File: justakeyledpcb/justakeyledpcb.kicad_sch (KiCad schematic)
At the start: 14 parts, among them SW1 SW_Push, SW2 SW_Push, SW3 SW_Push, SW4 SW_Push, U1 XIAO-RP2040-DIP

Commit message: The Schematic is Finalised
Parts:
- added R5: R, Resistor_THT:R_Axial_DIN0207_L6.3mm_D2.5mm_P7.62mm_Horizontal, symbol Device:R
- BZ1: footprint (none) -> Buzzer_Beeper:Buzzer_12x9.5RM7.6
- D1, D2, D3, D4: footprint (none) -> footprints:LEDRD254W57D500H1070
- R1, R2, R3, R4: footprint (none) -> Resistor_THT:R_Axial_DIN0207_L6.3mm_D2.5mm_P7.62mm_Horizontal
- SW1, SW2, SW3, SW4: footprint (none) -> Button_Switch_Keyboard:SW_Cherry_MX_1.00u_PCB
- U1: footprint Module:MOUDLE14P-XIAO-DIP-SMD -> footprints:XIAO-RP2040-DIP
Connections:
- net Buzzer: now also R5.1; no longer BZ1.1 (+)
- new net: BZ1.1 (+), R5.2
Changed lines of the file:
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@@
 	(wire
 		(pts
-			(xy 162.56 72.39) (xy 167.64 72.39)
+			(xy 99.06 78.74) (xy 102.87 78.74)
 		)
 		(stroke
@@
 	(wire
 		(pts
-			(xy 99.06 78.74) (xy 102.87 78.74)
+			(xy 99.06 74.93) (xy 102.87 74.93)
 		)
 		(stroke
@@
 	(wire
 		(pts
-			(xy 99.06 74.93) (xy 102.87 74.93)
+			(xy 138.43 86.36) (xy 140.97 86.36)
 		)
 		(stroke
@@
 	(wire
 		(pts
-			(xy 138.43 86.36) (xy 140.97 86.36)
+			(xy 133.35 49.53) (xy 130.81 49.53)
 		)
 		(stroke
@@
 	(wire
 		(pts
-			(xy 133.35 49.53) (xy 130.81 49.53)
+			(xy 138.43 93.98) (xy 140.97 93.98)
 		)
 		(stroke
@@
 	(wire
 		(pts
-			(xy 138.43 93.98) (xy 140.97 93.98)
+			(xy 99.06 82.55) (xy 102.87 82.55)
 		)
 		(stroke
@@
 	(wire
 		(pts
-			(xy 99.06 82.55) (xy 102.87 82.55)
+			(xy 138.43 74.93) (xy 146.05 74.93)
 		)
 		(stroke
@@
 	(wire
 		(pts
-			(xy 138.43 74.93) (xy 146.05 74.93)
+			(xy 138.43 82.55) (xy 140.97 82.55)
 		)
 		(stroke
@@
 	(wire
 		(pts
-			(xy 138.43 82.55) (xy 140.97 82.55)
+			(xy 99.06 71.12) (xy 102.87 71.12)
 		)
 		(stroke
@@
 		)
 	)
-	(wire
-		(pts
-			(xy 99.06 71.12) (xy 102.87 71.12)
-		)
-		(stroke
-			(width 0)
-			(type default)
-		)
-	)
 	(global_label "LED 1"
 		(shape input)
@@
 	(global_label "Buzzer"
 		(shape input)
-		(at 162.56 72.39 180)
+		(at 160.02 72.39 180)
 		(fields_autoplaced yes)
 		(effects
@@
 		)
 		(property "Intersheetrefs" "${INTERSHEET_REFS}"
-			(at 153.2248 72.39 0)
+			(at 150.6848 72.39 0)
 			(effects
 				(font
@@
 			)
 		)
-		(property "Footprint" ""
+		(property "Footprint" "Button_Switch_Keyboard:SW_Cherry_MX_1.00u_PCB"
 			(at 125.73 44.45 0)
 			(effects
@@
 			)
 		)
-		(property "Footprint" ""
+		(property "Footprint" "Resistor_THT:R_Axial_DIN0207_L6.3mm_D2.5mm_P7.62mm_Horizontal"
 			(at 165.1 57.658 90)
 			(effects
@@
 			)
 		)
-		(property "Footprint" ""
+		(property "Footprint" "footprints:LEDRD254W57D500H1070"
 			(at 172.72 55.88 0)
 			(effects
@@
 			)
 		)
-		(property "Footprint" ""
+		(property "Footprint" "Button_Switch_Keyboard:SW_Cherry_MX_1.00u_PCB"
 			(at 125.73 33.02 0)
 			(effects
@@
 			)
 		)
-		(property "Footprint" "Module:MOUDLE14P-XIAO-DIP-SMD"
+		(property "Footprint" "footprints:XIAO-RP2040-DIP"
 			(at 121.158 98.298 0)
 			(effects
@@
 			)
 		)
-		(property "Footprint" ""
+		(property "Footprint" "Resistor_THT:R_Axial_DIN0207_L6.3mm_D2.5mm_P7.62mm_Horizontal"
 			(at 165.1 66.548 90)
 			(effects
@@
 			)
 		)
-		(property "Footprint" ""
+		(property "Footprint" "Buzzer_Beeper:Buzzer_12x9.5RM7.6"
 			(at 167.64 74.295 90)
 			(effects
@@
 			)
 		)
-		(property "Footprint" ""
+		(property "Footprint" "footprints:LEDRD254W57D500H1070"
 			(at 172.72 64.77 0)
 			(effects
@@
 			)
 		)
-		(property "Footprint" ""
+		(property "Footprint" "Resistor_THT:R_Axial_DIN0207_L6.3mm_D2.5mm_P7.62mm_Horizontal"
 			(at 165.1 39.878 90)
 			(effects
@@
 			)
 		)
-		(property "Footprint" ""
+		(property "Footprint" "footprints:LEDRD254W57D500H1070"
 			(at 172.72 38.1 0)
 			(effects
@@
 			)
 		)
-		(property "Footprint" ""
+		(property "Footprint" "Button_Switch_Keyboard:SW_Cherry_MX_1.00u_PCB"
 			(at 107.95 30.48 0)
 			(effects
@@
 			)
 		)
-		(property "Footprint" ""
+		(property "Footprint" "Resistor_THT:R_Axial_DIN0207_L6.3mm_D2.5mm_P7.62mm_Horizontal"
 			(at 165.1 48.768 90)
 			(effects
@@
 			)
 		)
-		(property "Footprint" ""
+		(property "Footprint" "Button_Switch_Keyboard:SW_Cherry_MX_1.00u_PCB"
 			(at 107.95 44.45 0)
 			(effects
@@
 	)
 	(symbol
+		(lib_id "Device:R")
+		(at 163.83 72.39 90)
+		(unit 1)
+		(exclude_from_sim no)
+		(in_bom yes)
+		(on_board yes)
+		(dnp no)
+		(fields_autoplaced yes)
+		(property "Reference" "R5"
+			(at 163.83 66.04 90)
+			(effects
+				(font
+					(size 1.27 1.27)
+				)
+			)
+		)
+		(property "Value" "R"
+			(at 163.83 68.58 90)
+			(effects
+				(font
+					(size 1.27 1.27)
+				)
+			)
+		)
+		(property "Footprint" "Resistor_THT:R_Axial_DIN0207_L6.3mm_D2.5mm_P7.62mm_Horizontal"
+			(at 163.83 74.168 90)
+			(effects
+				(font
+					(size 1.27 1.27)
+				)
+				(hide yes)
+			)
+		)
+		(property "Datasheet" "~"
+			(at 163.83 72.39 0)
+			(effects
+				(font
+					(size 1.27 1.27)
+				)
+				(hide yes)
+			)
+		)
+		(property "Description" "Resistor"
+			(at 163.83 72.39 0)
+			(effects
+				(font
+					(size 1.27 1.27)
+				)
+				(hide yes)
+			)
+		)
+		(pin "2"
+		)
+		(pin "1"
+		)
+		(instances
+			(project ""
+				(path "/15b9dd11-e1bc-4be5-bc48-736a919b65d9"
+					(reference "R5")
+					(unit 1)
+				)
+			)
+		)
+	)
+	(symbol
 		(lib_id "power:GND")
 		(at 113.03 49.53 0)
@@
 			)
 		)
-		(property "Footprint" ""
+		(property "Footprint" "footprints:LEDRD254W57D500H1070"
 			(at 172.72 46.99 0)
 			(effects

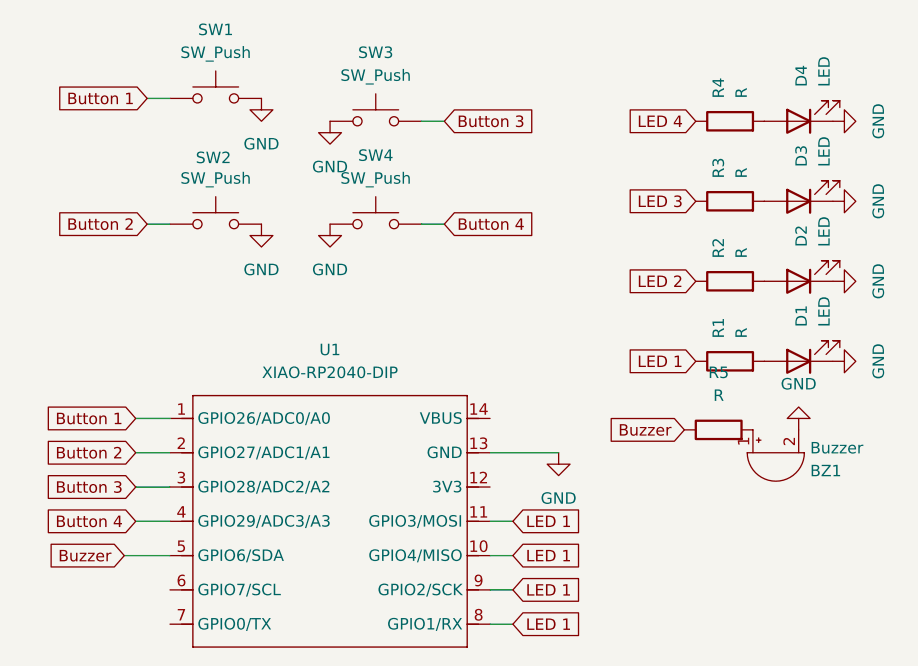
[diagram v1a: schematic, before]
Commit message: Added the LED's footprints properly
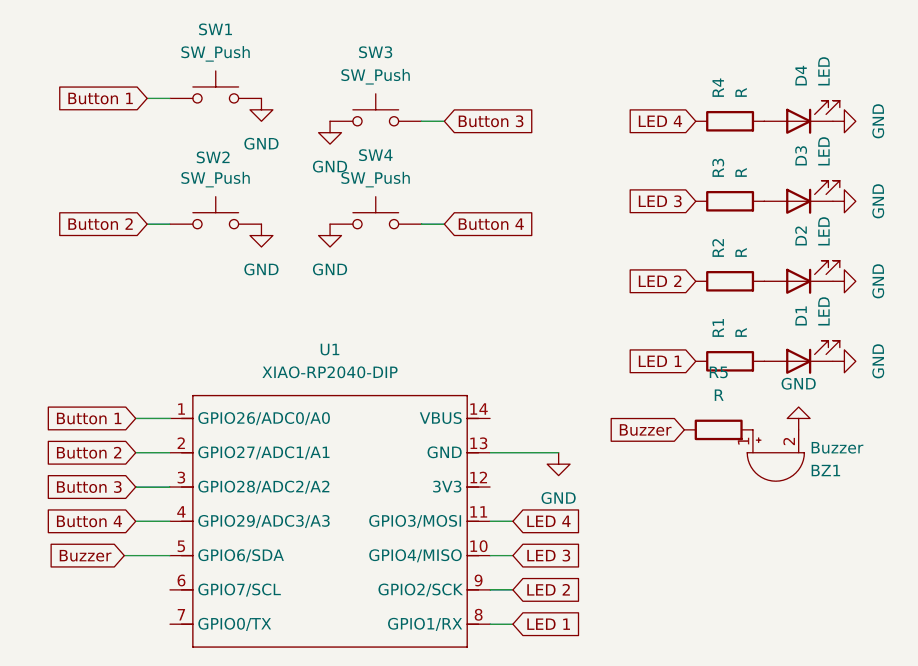
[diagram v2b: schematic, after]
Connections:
- net LED 1: no longer U1.10 (GPIO4/MISO), U1.11 (GPIO3/MOSI), U1.9 (GPIO2/SCK)
- net LED 2: now also U1.9 (GPIO2/SCK)
- net LED 3: now also U1.10 (GPIO4/MISO)
- net LED 4: now also U1.11 (GPIO3/MOSI)

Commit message: FInalised the PCB Schematics and PCB Layout
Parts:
- removed D1, D2, D3, D4: LED, footprints:LEDRD254W57D500H1070, symbol Device:LED
- added D1, D2, D3, D4: L08R5000Q1, e390cee6c564169ed6d49fe7a268946ec8897500_l08r5000q1:LEDRD254W57D500H1070, symbol L08R5000Q1:L08R5000Q1
- renumbered R5 to R1, R1 to R5
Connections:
- net GND: now also D1.C, D2.C, D3.C, D4.C
- net at R2.2: now also D3.A
- net at R5.2: now also D4.A
- net at R4.2: now also D1.A
- net at R3.2: now also D2.A
